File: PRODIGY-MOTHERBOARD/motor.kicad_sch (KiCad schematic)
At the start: 1 part, among them U13 DRV8870DDA

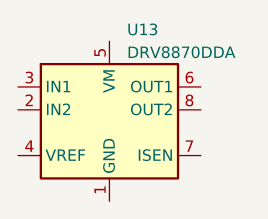
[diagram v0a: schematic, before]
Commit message: project restructure done. Hierarchical sheet done. Outputs/breakouts sheet done
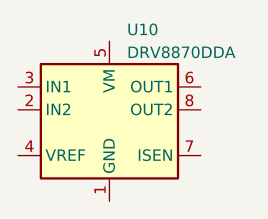
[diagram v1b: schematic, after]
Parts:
- renumbered U13 to U10
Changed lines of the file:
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@@
-(kicad_sch (version 20230121) (generator eeschema)
-  (paper "A4")
-  (symbol (lib_id "Driver_Motor:DRV8870DDA") (at 142.24 91.44 0) (unit 1)
-    (in_bom yes) (on_board yes) (dnp no) (fields_autoplaced)
-    (property "Reference" "U13" (at 144.1959 82.55 0)
-      (effects (font (size 1.27 1.27)) (justify left))
-    )
-    (property "Value" "DRV8870DDA" (at 144.1959 85.09 0)
-      (effects (font (size 1.27 1.27)) (justify left))
-    )
-    (property "Footprint" "Package_SO:Texas_HTSOP-8-1EP_3.9x4.9mm_P1.27mm_EP2.95x4.9mm_Mask2.4x3.1mm_ThermalVias" (at 144.78 93.98 0)
-      (effects (font (size 1.27 1.27)) hide)
-    )
-    (property "Datasheet" "http://www.ti.com/lit/ds/symlink/drv8870.pdf" (at 135.89 82.55 0)
-      (effects (font (size 1.27 1.27)) hide)
-    )
-    (pin "1")
-    (pin "2")
-    (pin "3")
-    (pin "4")
-    (pin "5")
-    (pin "6")
-    (pin "7")
-    (pin "8")
-    (pin "9")
-    (instances
-      (project "PRODIGY-MOTHERBOARD"
-        (path "/f1c25860-8989-4190-bd24-2491d23ca7d9/68c611b4-6626-4f5e-8db6-2b7527a0fa95"
-          (reference "U13") (unit 1)
-        )
-      )
-    )
-  )
+(kicad_sch
+	(version 20231120)
+	(generator "eeschema")
+	(generator_version "8.0")
+	(paper "A4")
+	(symbol
+		(lib_id "Driver_Motor:DRV8870DDA")
+		(at 142.24 91.44 0)
+		(unit 1)
+		(exclude_from_sim no)
+		(in_bom yes)
+		(on_board yes)
+		(dnp no)
+		(fields_autoplaced yes)
+		(property "Reference" "U10"
+			(at 144.1959 82.55 0)
+			(effects
+				(font
+					(size 1.27 1.27)
+				)
+				(justify left)
+			)
+		)
+		(property "Value" "DRV8870DDA"
+			(at 144.1959 85.09 0)
+			(effects
+				(font
+					(size 1.27 1.27)
+				)
+				(justify left)
+			)
+		)
+		(property "Footprint" "Package_SO:Texas_HTSOP-8-1EP_3.9x4.9mm_P1.27mm_EP2.95x4.9mm_Mask2.4x3.1mm_ThermalVias"
+			(at 144.78 93.98 0)
+			(effects
+				(font
+					(size 1.27 1.27)
+				)
+				(hide yes)
+			)
+		)
+		(property "Datasheet" "http://www.ti.com/lit/ds/symlink/drv8870.pdf"
+			(at 135.89 82.55 0)
+			(effects
+				(font
+					(size 1.27 1.27)
+				)
+				(hide yes)
+			)
+		)
+		(property "Description" ""
+			(at 142.24 91.44 0)
+			(effects
+				(font
+					(size 1.27 1.27)
+				)
+				(hide yes)
+			)
+		)
+		(pin "1"
+		)
+		(pin "2"
+		)
+		(pin "3"
+		)
+		(pin "4"
+		)
+		(pin "5"
+		)
+		(pin "6"
+		)
+		(pin "7"
+		)
+		(pin "8"
+		)
+		(pin "9"
+		)
+		(instances
+			(project "PRODIGY-MOTHERBOARD"
+				(path "/f1c25860-8989-4190-bd24-2491d23ca7d9/68c611b4-6626-4f5e-8db6-2b7527a0fa95"
+					(reference "U10")
+					(unit 1)
+				)
+			)
+		)
+	)
 )

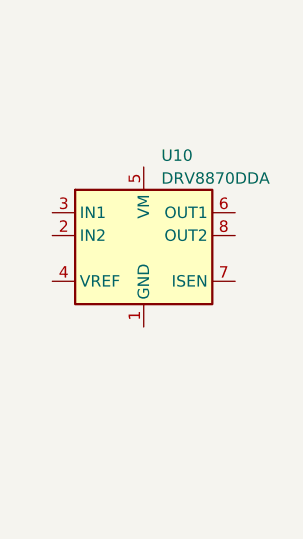
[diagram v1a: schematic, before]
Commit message: Finished I2C device and bus schematics. Added logic level translation.
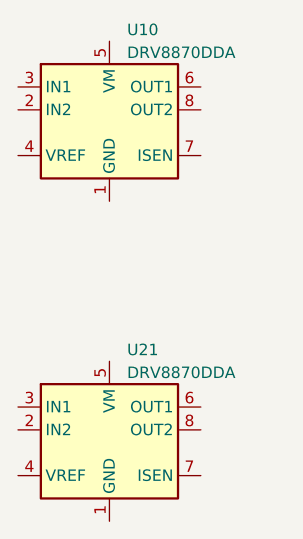
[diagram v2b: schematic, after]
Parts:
- added U21: DRV8870DDA, Package_SO:Texas_HTSOP-8-1EP_3.9x4.9mm_P1.27mm_EP2.95x4.9mm_Mask2.4x3.1mm_ThermalVias, symbol Driver_Motor:DRV8870DDA
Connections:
- new net: U21.1 (GND), U21.9 (GND)
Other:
- moved on the sheet: U10
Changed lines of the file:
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@@
 	(symbol
 		(lib_id "Driver_Motor:DRV8870DDA")
-		(at 142.24 91.44 0)
+		(at 138.43 113.03 0)
 		(unit 1)
 		(exclude_from_sim no)
@@
 		(dnp no)
 		(fields_autoplaced yes)
-		(property "Reference" "U10"
-			(at 144.1959 82.55 0)
+		(property "Reference" "U21"
+			(at 140.3859 104.14 0)
 			(effects
 				(font
@@
 		)
 		(property "Value" "DRV8870DDA"
-			(at 144.1959 85.09 0)
+			(at 140.3859 106.68 0)
 			(effects
 				(font
@@
 		)
 		(property "Footprint" "Package_SO:Texas_HTSOP-8-1EP_3.9x4.9mm_P1.27mm_EP2.95x4.9mm_Mask2.4x3.1mm_ThermalVias"
-			(at 144.78 93.98 0)
+			(at 140.97 115.57 0)
 			(effects
 				(font
@@
 		)
 		(property "Datasheet" "http://www.ti.com/lit/ds/symlink/drv8870.pdf"
-			(at 135.89 82.55 0)
+			(at 132.08 104.14 0)
 			(effects
 				(font
@@
 		)
 		(property "Description" ""
-			(at 142.24 91.44 0)
+			(at 138.43 113.03 0)
 			(effects
 				(font
+					(size 1.27 1.27)
+				)
+				(hide yes)
+			)
+		)
+		(pin "1"
+		)
+		(pin "2"
+		)
+		(pin "3"
+		)
+		(pin "4"
+		)
+		(pin "5"
+		)
+		(pin "6"
+		)
+		(pin "7"
+		)
+		(pin "8"
+		)
+		(pin "9"
+		)
+		(instances
+			(project "PRODIGY-MOTHERBOARD"
+				(path "/f1c25860-8989-4190-bd24-2491d23ca7d9/68c611b4-6626-4f5e-8db6-2b7527a0fa95"
+					(reference "U21")
+					(unit 1)
+				)
+			)
+		)
+	)
+	(symbol
+		(lib_id "Driver_Motor:DRV8870DDA")
+		(at 138.43 77.47 0)
+		(unit 1)
+		(exclude_from_sim no)
+		(in_bom yes)
+		(on_board yes)
+		(dnp no)
+		(fields_autoplaced yes)
+		(property "Reference" "U10"
+			(at 140.3859 68.58 0)
+			(effects
+				(font
+					(size 1.27 1.27)
+				)
+				(justify left)
+			)
+		)
+		(property "Value" "DRV8870DDA"
+			(at 140.3859 71.12 0)
+			(effects
+				(font
+					(size 1.27 1.27)
+				)
+				(justify left)
+			)
+		)
+		(property "Footprint" "Package_SO:Texas_HTSOP-8-1EP_3.9x4.9mm_P1.27mm_EP2.95x4.9mm_Mask2.4x3.1mm_ThermalVias"
+			(at 140.97 80.01 0)
+			(effects
+				(font
+					(size 1.27 1.27)
+				)
+				(hide yes)
+			)
+		)
+		(property "Datasheet" "http://www.ti.com/lit/ds/symlink/drv8870.pdf"
+			(at 132.08 68.58 0)
+			(effects
+				(font
+					(size 1.27 1.27)
+				)
+				(hide yes)
+			)
+		)
+		(property "Description" ""
+			(at 138.43 77.47 0)
+			(effects
+				(font

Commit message: CAN schematic done
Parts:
- removed U21: DRV8870DDA, Package_SO:Texas_HTSOP-8-1EP_3.9x4.9mm_P1.27mm_EP2.95x4.9mm_Mask2.4x3.1mm_ThermalVias, symbol Driver_Motor:DRV8870DDA
- added C28, C29: 47uF, Capacitor_SMD:CP_Elec_6.3x5.8, symbol Device:C_Polarized
- added C30, C31: 100nF, symbol Device:C
- added R23, R24: 2, Resistor_SMD:R_2512_6332Metric, symbol Device:R
- added U12: DRV8870DDA, Package_SO:Texas_HTSOP-8-1EP_3.9x4.9mm_P1.27mm_EP2.95x4.9mm_Mask2.4x3.1mm_ThermalVias, symbol Driver_Motor:DRV8870DDA
- renumbered U10 to U11
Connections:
- net GND: now reaches U11.1 (GND), U11.9 (GND)
- net GND: now also C28.2, C29.2, C30.2, C31.2, R23.2, R24.2, U12.1 (GND), U12.9 (GND)
- net MOTOR_IN2_1: now reaches U11.2 (IN2)
- net MOTOR_IN1_1: now reaches U11.3 (IN1)
- net +3.3V: now reaches U11.4 (VREF)
- net +3.3V: now also U12.4 (VREF)
- net +12V: now reaches U11.5 (VM)
- net +12V: now also C28.1, C29.1, C30.1, C31.1, U12.5 (VM)
- net MOTOR_OUT1_BREAKOUT_1: now reaches U11.6 (OUT1)
- net at U11.7 (ISEN): now also R23.1
- net MOTOR_OUT2_BREAKOUT_1: now reaches U11.8 (OUT2)
- new net: R24.1, U12.7 (ISEN)
- new net MOTOR_IN1_2: U12.3 (IN1)
- new net MOTOR_IN2_2: U12.2 (IN2)
- new net MOTOR_OUT1_BREAKOUT_2: U12.6 (OUT1)
- new net MOTOR_OUT2_BREAKOUT_2: U12.8 (OUT2)
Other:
- note added: "I^2 * R = 0.5W I = 0.5A"

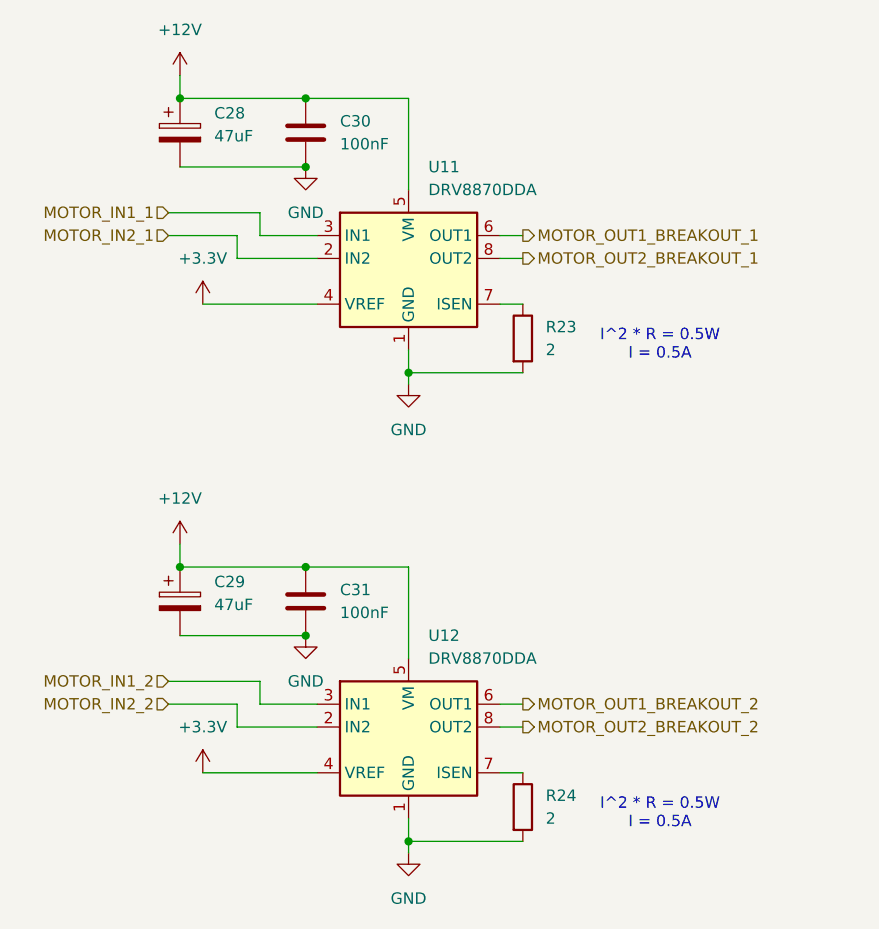
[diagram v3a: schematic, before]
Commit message: SPI NFC schematic done.
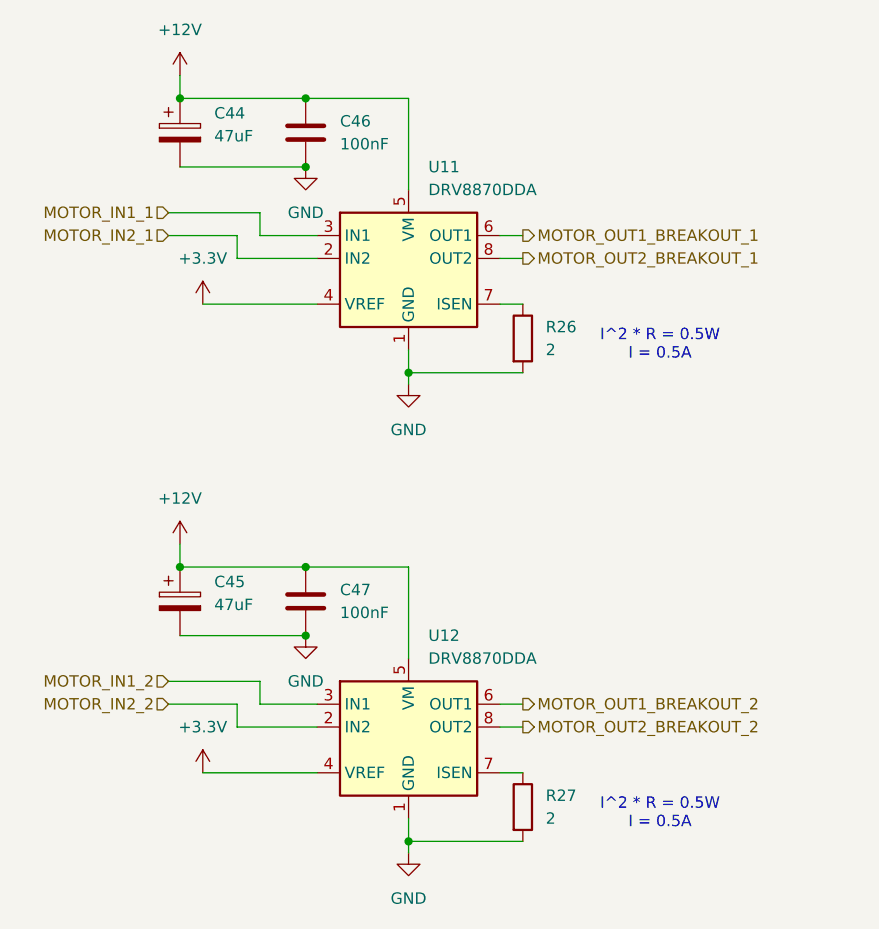
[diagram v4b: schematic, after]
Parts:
- renumbered C28 to C44, C29 to C45, C30 to C46, C31 to C47, R23 to R26, R24 to R27
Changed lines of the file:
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@@
 		(dnp no)
 		(fields_autoplaced yes)
-		(property "Reference" "#PWR049"
+		(property "Reference" "#PWR064"
 			(at 127 125.73 0)
 			(effects
@@
 			(project "PRODIGY-MOTHERBOARD"
 				(path "/f1c25860-8989-4190-bd24-2491d23ca7d9/68c611b4-6626-4f5e-8db6-2b7527a0fa95"
-					(reference "#PWR049")
+					(reference "#PWR064")
 					(unit 1)
 				)
@@
 		(dnp no)
 		(fields_autoplaced yes)
-		(property "Reference" "#PWR045"
+		(property "Reference" "#PWR060"
 			(at 113.03 113.03 0)
 			(effects
@@
 			(project "PRODIGY-MOTHERBOARD"
 				(path "/f1c25860-8989-4190-bd24-2491d23ca7d9/68c611b4-6626-4f5e-8db6-2b7527a0fa95"
-					(reference "#PWR045")
+					(reference "#PWR060")
 					(unit 1)
 				)
@@
 		(dnp no)
 		(fields_autoplaced yes)
-		(property "Reference" "C31"
+		(property "Reference" "C47"
 			(at 130.81 114.2999 0)
 			(effects
@@
 			(project "PRODIGY-MOTHERBOARD"
 				(path "/f1c25860-8989-4190-bd24-2491d23ca7d9/68c611b4-6626-4f5e-8db6-2b7527a0fa95"
-					(reference "C31")
+					(reference "C47")
 					(unit 1)
 				)
@@
 		(dnp no)
 		(fields_autoplaced yes)
-		(property "Reference" "R24"
+		(property "Reference" "R27"
 			(at 153.67 137.1599 0)
 			(effects
@@
 			(project "PRODIGY-MOTHERBOARD"
 				(path "/f1c25860-8989-4190-bd24-2491d23ca7d9/68c611b4-6626-4f5e-8db6-2b7527a0fa95"
-					(reference "R24")
+					(reference "R27")
 					(unit 1)
 				)
@@
 		(dnp no)
 		(fields_autoplaced yes)
-		(property "Reference" "#PWR044"
+		(property "Reference" "#PWR059"
 			(at 113.03 60.96 0)
 			(effects
@@
 			(project "PRODIGY-MOTHERBOARD"
 				(path "/f1c25860-8989-4190-bd24-2491d23ca7d9/68c611b4-6626-4f5e-8db6-2b7527a0fa95"
-					(reference "#PWR044")
+					(reference "#PWR059")
 					(unit 1)
 				)
@@
 		(dnp no)
 		(fields_autoplaced yes)
-		(property "Reference" "#PWR051"
+		(property "Reference" "#PWR066"
 			(at 138.43 149.86 0)
 			(effects
@@
 			(project "PRODIGY-MOTHERBOARD"
 				(path "/f1c25860-8989-4190-bd24-2491d23ca7d9/68c611b4-6626-4f5e-8db6-2b7527a0fa95"
-					(reference "#PWR051")
+					(reference "#PWR066")
 					(unit 1)
 				)
@@
 		(dnp no)
 		(fields_autoplaced yes)
-		(property "Reference" "R23"
+		(property "Reference" "R26"
 			(at 153.67 85.0899 0)
 			(effects
@@
 			(project "PRODIGY-MOTHERBOARD"
 				(path "/f1c25860-8989-4190-bd24-2491d23ca7d9/68c611b4-6626-4f5e-8db6-2b7527a0fa95"
-					(reference "R23")
+					(reference "R26")
 					(unit 1)
 				)
@@
 		(dnp no)
 		(fields_autoplaced yes)
-		(property "Reference" "#PWR050"
+		(property "Reference" "#PWR065"
 			(at 138.43 97.79 0)
 			(effects
@@
 			(project "PRODIGY-MOTHERBOARD"
 				(path "/f1c25860-8989-4190-bd24-2491d23ca7d9/68c611b4-6626-4f5e-8db6-2b7527a0fa95"
-					(reference "#PWR050")
+					(reference "#PWR065")
 					(unit 1)
 				)
@@
 		(dnp no)
 		(fields_autoplaced yes)
-		(property "Reference" "C28"
+		(property "Reference" "C44"
 			(at 116.84 61.3409 0)
 			(effects
@@
 			(project "PRODIGY-MOTHERBOARD"
 				(path "/f1c25860-8989-4190-bd24-2491d23ca7d9/68c611b4-6626-4f5e-8db6-2b7527a0fa95"
-					(reference "C28")
+					(reference "C44")
 					(unit 1)
 				)
@@
 		(dnp no)
 		(fields_autoplaced yes)
-		(property "Reference" "C30"
+		(property "Reference" "C46"
 			(at 130.81 62.2299 0)
 			(effects
@@
 			(project "PRODIGY-MOTHERBOARD"
 				(path "/f1c25860-8989-4190-bd24-2491d23ca7d9/68c611b4-6626-4f5e-8db6-2b7527a0fa95"
-					(reference "C30")
+					(reference "C46")
 					(unit 1)
 				)
@@
 		(dnp no)
 		(fields_autoplaced yes)
-		(property "Reference" "#PWR046"
+		(property "Reference" "#PWR061"
 			(at 115.57 86.36 0)
 			(effects
@@
 			(project "PRODIGY-MOTHERBOARD"
 				(path "/f1c25860-8989-4190-bd24-2491d23ca7d9/68c611b4-6626-4f5e-8db6-2b7527a0fa95"
-					(reference "#PWR046")
+					(reference "#PWR061")
 					(unit 1)
 				)
@@
 		(dnp no)
 		(fields_autoplaced yes)
-		(property "Reference" "#PWR048"
+		(property "Reference" "#PWR063"
 			(at 127 73.66 0)
 			(effects
@@
 			(project "PRODIGY-MOTHERBOARD"
 				(path "/f1c25860-8989-4190-bd24-2491d23ca7d9/68c611b4-6626-4f5e-8db6-2b7527a0fa95"
-					(reference "#PWR048")
+					(reference "#PWR063")
 					(unit 1)
 				)
@@
 		(dnp no)
 		(fields_autoplaced yes)
-		(property "Reference" "#PWR047"
+		(property "Reference" "#PWR062"
 			(at 115.57 138.43 0)
 			(effects
@@
 			(project "PRODIGY-MOTHERBOARD"
 				(path "/f1c25860-8989-4190-bd24-2491d23ca7d9/68c611b4-6626-4f5e-8db6-2b7527a0fa95"
-					(reference "#PWR047")
+					(reference "#PWR062")
 					(unit 1)
 				)
@@
 		(dnp no)
 		(fields_autoplaced yes)
-		(property "Reference" "C29"
+		(property "Reference" "C45"
 			(at 116.84 113.4109 0)
 			(effects
@@
 			(project "PRODIGY-MOTHERBOARD"
 				(path "/f1c25860-8989-4190-bd24-2491d23ca7d9/68c611b4-6626-4f5e-8db6-2b7527a0fa95"
-					(reference "C29")
-					(unit 1)
-				)
+					(reference "C45")
+					(unit 1)
+				)

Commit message: Added pins to MCU. Added Decoder for SPI SS-Multiplexing.
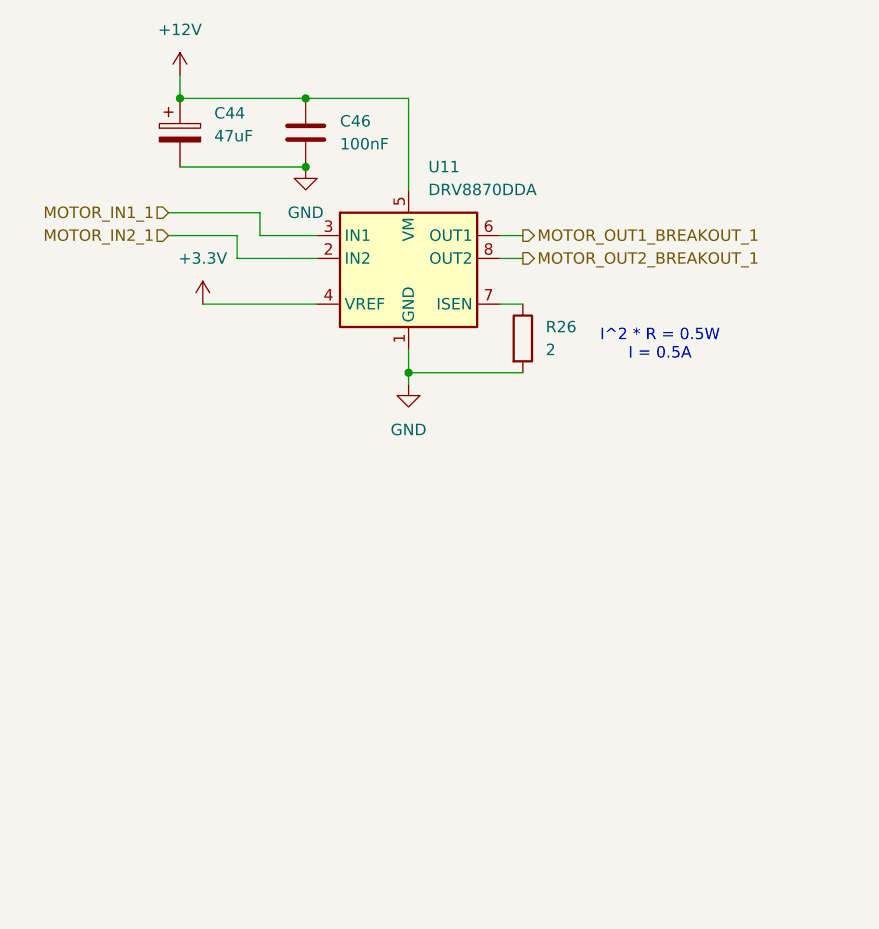
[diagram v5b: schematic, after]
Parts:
- removed C45: 47uF, Capacitor_SMD:CP_Elec_6.3x5.8, symbol Device:C_Polarized
- removed C47: 100nF, symbol Device:C
- removed R27: 2, Resistor_SMD:R_2512_6332Metric, symbol Device:R
- removed U12: DRV8870DDA, Package_SO:Texas_HTSOP-8-1EP_3.9x4.9mm_P1.27mm_EP2.95x4.9mm_Mask2.4x3.1mm_ThermalVias, symbol Driver_Motor:DRV8870DDA

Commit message: Added proper debounce filter elements to buttons.
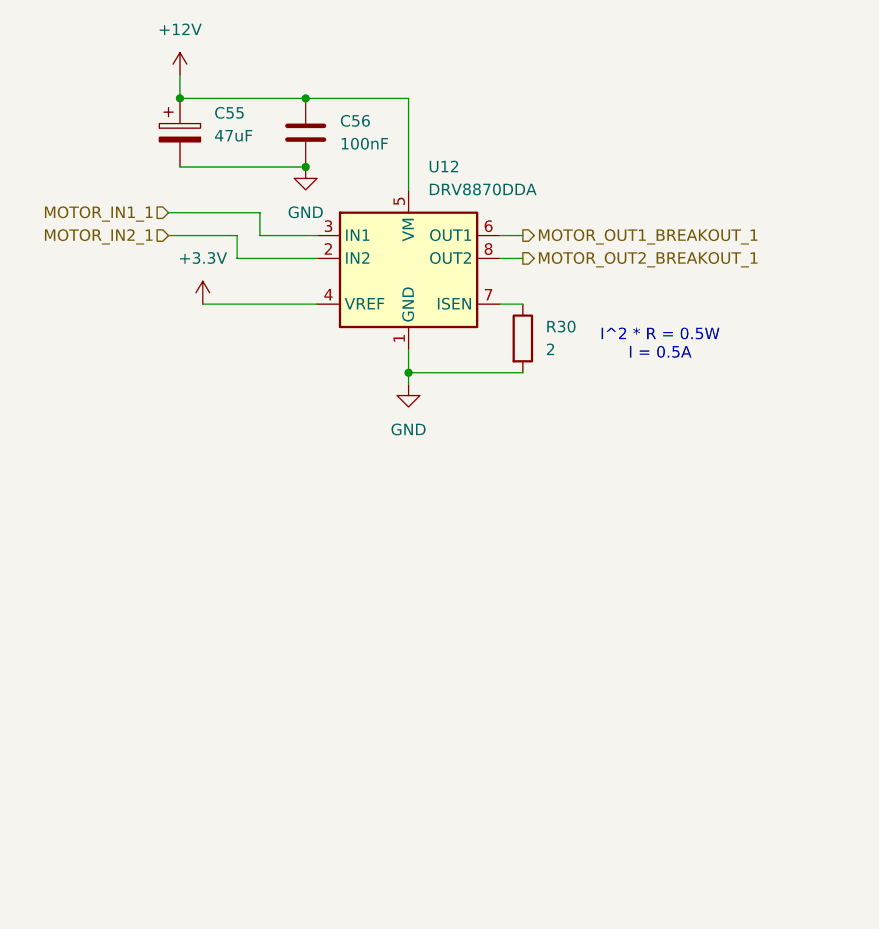
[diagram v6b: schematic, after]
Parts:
- renumbered C44 to C55, C46 to C56, R26 to R30, U11 to U12
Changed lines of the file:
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@@
 		(dnp no)
 		(fields_autoplaced yes)
-		(property "Reference" "#PWR059"
+		(property "Reference" "#PWR070"
 			(at 113.03 60.96 0)
 			(effects
@@
 			(project "PRODIGY-MOTHERBOARD"
 				(path "/f1c25860-8989-4190-bd24-2491d23ca7d9/68c611b4-6626-4f5e-8db6-2b7527a0fa95"
-					(reference "#PWR059")
+					(reference "#PWR070")
 					(unit 1)
 				)
@@
 		(dnp no)
 		(fields_autoplaced yes)
-		(property "Reference" "R26"
+		(property "Reference" "R30"
 			(at 153.67 85.0899 0)
 			(effects
@@
 			(project "PRODIGY-MOTHERBOARD"
 				(path "/f1c25860-8989-4190-bd24-2491d23ca7d9/68c611b4-6626-4f5e-8db6-2b7527a0fa95"
-					(reference "R26")
+					(reference "R30")
 					(unit 1)
 				)
@@
 		(dnp no)
 		(fields_autoplaced yes)
-		(property "Reference" "#PWR065"
+		(property "Reference" "#PWR073"
 			(at 138.43 97.79 0)
 			(effects
@@
 			(project "PRODIGY-MOTHERBOARD"
 				(path "/f1c25860-8989-4190-bd24-2491d23ca7d9/68c611b4-6626-4f5e-8db6-2b7527a0fa95"
-					(reference "#PWR065")
+					(reference "#PWR073")
 					(unit 1)
 				)
@@
 		(dnp no)
 		(fields_autoplaced yes)
-		(property "Reference" "C44"
+		(property "Reference" "C55"
 			(at 116.84 61.3409 0)
 			(effects
@@
 			(project "PRODIGY-MOTHERBOARD"
 				(path "/f1c25860-8989-4190-bd24-2491d23ca7d9/68c611b4-6626-4f5e-8db6-2b7527a0fa95"
-					(reference "C44")
+					(reference "C55")
 					(unit 1)
 				)
@@
 		(dnp no)
 		(fields_autoplaced yes)
-		(property "Reference" "C46"
+		(property "Reference" "C56"
 			(at 130.81 62.2299 0)
 			(effects
@@
 			(project "PRODIGY-MOTHERBOARD"
 				(path "/f1c25860-8989-4190-bd24-2491d23ca7d9/68c611b4-6626-4f5e-8db6-2b7527a0fa95"
-					(reference "C46")
+					(reference "C56")
 					(unit 1)
 				)
@@
 		(dnp no)
 		(fields_autoplaced yes)
-		(property "Reference" "#PWR061"
+		(property "Reference" "#PWR072"
 			(at 115.57 86.36 0)
 			(effects
@@
 			(project "PRODIGY-MOTHERBOARD"
 				(path "/f1c25860-8989-4190-bd24-2491d23ca7d9/68c611b4-6626-4f5e-8db6-2b7527a0fa95"
-					(reference "#PWR061")
+					(reference "#PWR072")
 					(unit 1)
 				)
@@
 		(dnp no)
 		(fields_autoplaced yes)
-		(property "Reference" "#PWR063"
+		(property "Reference" "#PWR071"
 			(at 127 73.66 0)
 			(effects
@@
 			(project "PRODIGY-MOTHERBOARD"
 				(path "/f1c25860-8989-4190-bd24-2491d23ca7d9/68c611b4-6626-4f5e-8db6-2b7527a0fa95"
-					(reference "#PWR063")
+					(reference "#PWR071")
 					(unit 1)
 				)
@@
 		(dnp no)
 		(fields_autoplaced yes)
-		(property "Reference" "U11"
+		(property "Reference" "U12"
 			(at 140.6241 67.31 0)
 			(effects
@@
 			(project "PRODIGY-MOTHERBOARD"
 				(path "/f1c25860-8989-4190-bd24-2491d23ca7d9/68c611b4-6626-4f5e-8db6-2b7527a0fa95"
-					(reference "U11")
-					(unit 1)
-				)
+					(reference "U12")
+					(unit 1)
+				)
